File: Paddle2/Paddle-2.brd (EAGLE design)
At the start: 68.6 x 53.3 mm, 9 parts

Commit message: Use internal counter and Schmitt trigger
* Switch to using internal 16 bit counter. Using a sequential increment
  was giving values that were too low since they were also taing time
  away from checking the input pin. TCNT1 runs in parallel and has 16bit
  precision. This gives values that (at 1/64f) are close to the 0-1023
  range the HID library wants. Atari wants 228 steps or so, so we're well
  over, but at least we're not below. This leaves the whole 16MHz frequency
  to do a read-compare-jump loop. Apparently it's like 4-6 clock cycles or
  something like that, which explains the huge incresea in precision.
* Use a Schmitt trigger. I couldn't find out much about ATMegaXX's hysteresis
  on digital input pins. There was some vague language that came with the
  warning that you can get into that nice transistor-y current overdraw
  state if you ramp up voltage into them. So... let's use a schmitt trigger
  to be safe. At least the 74HC14 was designed to live under these conditions.
* The loop timing should waste around 6-8ms which looks like the time
  needed to discharge the cap. Actual running conditions may vary. Also,
  I have literally no idea on the performance characteristics of the
  HID library, so I guess we can tinker with this value some more in the
  future.
  This kinda boils down to, what, 8*4=32ms cycle to read both paddles.
  Which is like 32Hz. Wait, that's slower than it should be. Hm...
  FIXME, maybe use draining circuit on cap to discharge it faster.
  Or just YOLO it and drop the cycle down 5ms including all the faffing
  about to get to 20ms ~ 50Hz. Maybe we can do better. Maybe. We'll see.
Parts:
- added U2: (no value), AUTODESK_CIRCUITS_BREADBOARD:DIL14
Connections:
- new net N$10: R1.1, U2.2
- new net N$11: U1.5V, U2.14
- new net N$9: R2.1, U2.8
- net N$2: now also U2.7
- net N$3: now also U2.1; no longer R1.1
- net N$7: now also U2.9; no longer R2.1
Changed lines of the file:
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@@
 </autorouter>
 <elements>
-<element value="" name="U1" library="AUTODESK_CIRCUITS_BREADBOARD" package="ARDUINO_UNO" x="5" y="10.08"></element><element value="4.7nF" name="C1" library="AUTODESK_CIRCUITS_BREADBOARD" package="C5B2.5" x="5" y="22.78"></element><element value="1k‎Ω" name="R1" library="AUTODESK_CIRCUITS_BREADBOARD" package="0207/10" x="5" y="35.480000000000004"></element><element value="1000k‎Ω" name="Rpot1" library="AUTODESK_CIRCUITS_BREADBOARD" package="B25V" x="5" y="48.18"></element><element value="" name="S1" library="AUTODESK_CIRCUITS_BREADBOARD" package="TL1105" x="5" y="60.879999999999995"></element><element value="1000k‎Ω" name="Rpot2" library="AUTODESK_CIRCUITS_BREADBOARD" package="B25V" x="5" y="73.58"></element><element value="1k‎Ω" name="R2" library="AUTODESK_CIRCUITS_BREADBOARD" package="0207/10" x="5" y="86.28"></element><element value="4.7nF" name="C2" library="AUTODESK_CIRCUITS_BREADBOARD" package="C5B2.5" x="5" y="98.98"></element><element value="" name="S2" library="AUTODESK_CIRCUITS_BREADBOARD" package="TL1105" x="5" y="111.68"></element></elements>
+<element value="" name="U1" library="AUTODESK_CIRCUITS_BREADBOARD" package="ARDUINO_UNO" x="5" y="10.08"></element><element value="4.7nF" name="C1" library="AUTODESK_CIRCUITS_BREADBOARD" package="C5B2.5" x="5" y="22.78"></element><element value="1k‎Ω" name="R1" library="AUTODESK_CIRCUITS_BREADBOARD" package="0207/10" x="5" y="35.480000000000004"></element><element value="1000k‎Ω" name="Rpot1" library="AUTODESK_CIRCUITS_BREADBOARD" package="B25V" x="5" y="48.18"></element><element value="" name="S1" library="AUTODESK_CIRCUITS_BREADBOARD" package="TL1105" x="5" y="60.879999999999995"></element><element value="1000k‎Ω" name="Rpot2" library="AUTODESK_CIRCUITS_BREADBOARD" package="B25V" x="5" y="73.58"></element><element value="1k‎Ω" name="R2" library="AUTODESK_CIRCUITS_BREADBOARD" package="0207/10" x="5" y="86.28"></element><element value="4.7nF" name="C2" library="AUTODESK_CIRCUITS_BREADBOARD" package="C5B2.5" x="5" y="98.98"></element><element value="" name="S2" library="AUTODESK_CIRCUITS_BREADBOARD" package="TL1105" x="5" y="111.68"></element><element value="" name="U2" library="AUTODESK_CIRCUITS_BREADBOARD" package="DIL14" x="5" y="124.38000000000001"></element></elements>
 <signals>
-<signal name="N$1"><contactref element="R1" pad="2"></contactref><contactref element="U1" pad="A0"></contactref><wire x1="10.08" y1="35.480000000000004" x2="55.8" y2="12.620000000000001" width="0" layer="19" extent="1-1"></wire></signal><signal name="N$2"><contactref element="U1" pad="GND.."></contactref><contactref element="C1" pad="2"></contactref><wire x1="45.64" y1="12.620000000000001" x2="7.54" y2="22.78" width="0" layer="19" extent="1-1"></wire><contactref element="S1" pad="2"></contactref><wire x1="7.54" y1="22.78" x2="7.25" y2="64.13" width="0" layer="19" extent="1-1"></wire><contactref element="C2" pad="2"></contactref><wire x1="7.25" y1="64.13" x2="7.54" y2="98.98" width="0" layer="19" extent="1-1"></wire><contactref element="S2" pad="2"></contactref><wire x1="7.54" y1="98.98" x2="7.25" y2="114.93" width="0" layer="19" extent="1-1"></wire></signal><signal name="N$3"><contactref element="C1" pad="1"></contactref><contactref element="R1" pad="1"></contactref><wire x1="2.46" y1="22.78" x2="-0.08000000000000007" y2="35.480000000000004" width="0" layer="19" extent="1-1"></wire><contactref element="Rpot1" pad="E"></contactref><wire x1="-0.08000000000000007" y1="35.480000000000004" x2="2.46" y2="48.815" width="0" layer="19" extent="1-1"></wire></signal><signal name="N$4"><contactref element="S1" pad="1"></contactref><contactref element="U1" pad="7"></contactref><wire x1="2.75" y1="64.13" x2="50.72" y2="60.879999999999995" width="0" layer="19" extent="1-1"></wire></signal><signal name="N$5"><contactref element="U1" pad="2"></contactref><contactref element="Rpot1" pad="S"></contactref><wire x1="63.42" y1="60.879999999999995" x2="5" y2="48.815" width="0" layer="19" extent="1-1"></wire><contactref element="Rpot2" pad="S"></contactref><wire x1="5" y1="48.815" x2="5" y2="74.215" width="0" layer="19" extent="1-1"></wire></signal><signal name="N$6"><contactref element="R2" pad="2"></contactref><contactref element="U1" pad="A1"></contactref><wire x1="10.08" y1="86.28" x2="58.34" y2="12.620000000000001" width="0" layer="19" extent="1-1"></wire></signal><signal name="N$7"><contactref element="Rpot2" pad="E"></contactref><contactref element="C2" pad="1"></contactref><wire x1="2.46" y1="74.215" x2="2.46" y2="98.98" width="0" layer="19" extent="1-1"></wire><contactref element="R2" pad="1"></contactref><wire x1="2.46" y1="98.98" x2="-0.08000000000000007" y2="86.28" width="0" layer="19" extent="1-1"></wire></signal><signal name="N$8"><contactref element="U1" pad="4"></contactref><contactref element="S2" pad="1"></contactref><wire x1="58.34" y1="60.879999999999995" x2="2.75" y2="114.93" width="0" layer="19" extent="1-1"></wire></signal></signals>
+<signal name="N$1"><contactref element="R1" pad="2"></contactref><contactref element="U1" pad="A0"></contactref><wire x1="10.08" y1="35.480000000000004" x2="55.8" y2="12.620000000000001" width="0" layer="19" extent="1-1"></wire></signal><signal name="N$2"><contactref element="U1" pad="GND.."></contactref><contactref element="C1" pad="2"></contactref><wire x1="45.64" y1="12.620000000000001" x2="7.54" y2="22.78" width="0" layer="19" extent="1-1"></wire><contactref element="S1" pad="2"></contactref><wire x1="7.54" y1="22.78" x2="7.25" y2="64.13" width="0" layer="19" extent="1-1"></wire><contactref element="C2" pad="2"></contactref><wire x1="7.25" y1="64.13" x2="7.54" y2="98.98" width="0" layer="19" extent="1-1"></wire><contactref element="S2" pad="2"></contactref><wire x1="7.54" y1="98.98" x2="7.25" y2="114.93" width="0" layer="19" extent="1-1"></wire><contactref element="U2" pad="7"></contactref><wire x1="7.25" y1="114.93" x2="12.620000000000001" y2="120.57000000000001" width="0" layer="19" extent="1-1"></wire></signal><signal name="N$3"><contactref element="C1" pad="1"></contactref><contactref element="Rpot1" pad="E"></contactref><wire x1="2.46" y1="22.78" x2="2.46" y2="48.815" width="0" layer="19" extent="1-1"></wire><contactref element="U2" pad="1"></contactref><wire x1="2.46" y1="48.815" x2="-2.62" y2="120.57000000000001" width="0" layer="19" extent="1-1"></wire></signal><signal name="N$4"><contactref element="S1" pad="1"></contactref><contactref element="U1" pad="7"></contactref><wire x1="2.75" y1="64.13" x2="50.72" y2="60.879999999999995" width="0" layer="19" extent="1-1"></wire></signal><signal name="N$5"><contactref element="U1" pad="2"></contactref><contactref element="Rpot1" pad="S"></contactref><wire x1="63.42" y1="60.879999999999995" x2="5" y2="48.815" width="0" layer="19" extent="1-1"></wire><contactref element="Rpot2" pad="S"></contactref><wire x1="5" y1="48.815" x2="5" y2="74.215" width="0" layer="19" extent="1-1"></wire></signal><signal name="N$6"><contactref element="R2" pad="2"></contactref><contactref element="U1" pad="A1"></contactref><wire x1="10.08" y1="86.28" x2="58.34" y2="12.620000000000001" width="0" layer="19" extent="1-1"></wire></signal><signal name="N$7"><contactref element="Rpot2" pad="E"></contactref><contactref element="C2" pad="1"></contactref><wire x1="2.46" y1="74.215" x2="2.46" y2="98.98" width="0" layer="19" extent="1-1"></wire><contactref element="U2" pad="9"></contactref><wire x1="2.46" y1="98.98" x2="10.08" y2="128.19" width="0" layer="19" extent="1-1"></wire></signal><signal name="N$8"><contactref element="U1" pad="4"></contactref><contactref element="S2" pad="1"></contactref><wire x1="58.34" y1="60.879999999999995" x2="2.75" y2="114.93" width="0" layer="19" extent="1-1"></wire></signal><signal name="N$9"><contactref element="U2" pad="8"></contactref><contactref element="R2" pad="1"></contactref><wire x1="12.620000000000001" y1="128.19" x2="-0.08000000000000007" y2="86.28" width="0" layer="19" extent="1-1"></wire></signal><signal name="N$10"><contactref element="U2" pad="2"></contactref><contactref element="R1" pad="1"></contactref><wire x1="-0.08000000000000007" y1="120.57000000000001" x2="-0.08000000000000007" y2="35.480000000000004" width="0" layer="19" extent="1-1"></wire></signal><signal name="N$11"><contactref element="U1" pad="5V"></contactref><contactref element="U2" pad="14"></contactref><wire x1="43.1" y1="12.620000000000001" x2="-2.62" y2="128.19" width="0" layer="19" extent="1-1"></wire></signal></signals>
 </board>
 </drawing>

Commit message: Add some series resistors; minor code updates
* force registers where there's no memory involved
* add ifdefs to toggle debug<->joystick mode
* get rid of some global variables
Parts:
- added R3, R4, R5, R6: 220‎Ω, AUTODESK_CIRCUITS_BREADBOARD:0207/10
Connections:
- new net N$12: R3.1, S1.2
- new net N$13: R5.1, S2.2
- new net N$14: R6.1, Rpot1.S
- new net N$15: R4.1, Rpot2.S
- net N$2: now also R3.2, R5.2; no longer S1.2, S2.2
- net N$5: now also R4.2, R6.2; no longer Rpot1.S, Rpot2.S

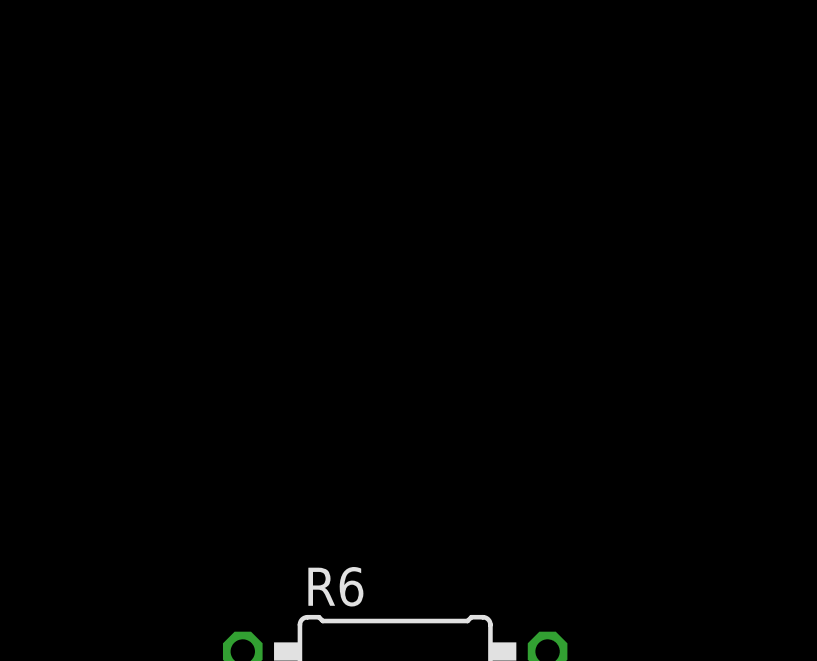
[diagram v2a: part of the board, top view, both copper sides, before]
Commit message: Clarify timing
* clarified timing
* switched to 2.2nF caps; if they don't work, "we have problem"
* added some extra .22k resistors
* some more documentation
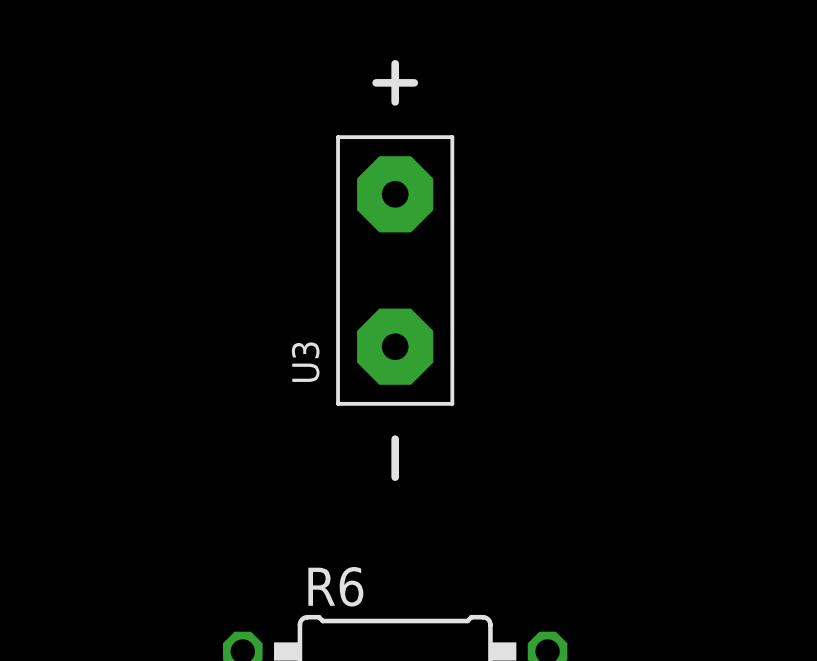
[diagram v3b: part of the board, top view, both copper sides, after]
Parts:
- added U3: (no value), AUTODESK_CIRCUITS_BREADBOARD:DC-POWER
- C1, C2: value 4.7nF -> 2.2nF
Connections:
- net N$2: now also U3.-
- net N$7: now also U3.+
